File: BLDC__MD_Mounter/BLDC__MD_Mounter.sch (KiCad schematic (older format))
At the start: 0 parts

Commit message: Placed Connectors on schematic
for Motor Driver, BLDC, Control and Power.
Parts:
- added J? (x8): Conn_02x07_Odd_Even, symbol Connector_Generic:Conn_02x07_Odd_Even
- added J? (x4): Conn_01x08_Female, symbol Connector:Conn_01x08_Female
- added J?: Conn_02x10_Odd_Even, symbol Connector_Generic:Conn_02x10_Odd_Even
- added J?: Conn_01x02_Male, symbol Connector:Conn_01x02_Male
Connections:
- new net +3V3: J?.1 (Pin_1), J?.5 (Pin_5), J?.5 (Pin_5), J?.5 (Pin_5), J?.5 (Pin_5)
- new net +5V: J?.10 (Pin_10), J?.10 (Pin_10), J?.10 (Pin_10), J?.10 (Pin_10), J?.3 (Pin_3), J?.6 (Pin_6), J?.6 (Pin_6), J?.6 (Pin_6), J?.6 (Pin_6), J?.9 (Pin_9), J?.9 (Pin_9), J?.9 (Pin_9), J?.9 (Pin_9)
- new net COIL_A_1: J?.5 (Pin_5), J?.6 (Pin_6)
- new net COIL_A_2: J?.5 (Pin_5), J?.6 (Pin_6)
- new net COIL_A_3: J?.5 (Pin_5), J?.6 (Pin_6)
- new net COIL_A_4: J?.5 (Pin_5), J?.6 (Pin_6)
- new net COIL_B_1: J?.10 (Pin_10), J?.9 (Pin_9)
- new net COIL_B_2: J?.10 (Pin_10), J?.9 (Pin_9)
- new net COIL_B_3: J?.10 (Pin_10), J?.9 (Pin_9)
- new net COIL_B_4: J?.10 (Pin_10), J?.9 (Pin_9)
- new net COIL_C_1: J?.7 (Pin_7), J?.8 (Pin_8)
- new net COIL_C_2: J?.7 (Pin_7), J?.8 (Pin_8)
- new net COIL_C_3: J?.7 (Pin_7), J?.8 (Pin_8)
- new net COIL_C_4: J?.7 (Pin_7), J?.8 (Pin_8)
- new net FG_1: J?.1 (Pin_1), J?.11 (Pin_11)
- new net FG_2: J?.1 (Pin_1), J?.19 (Pin_19)
- new net FG_3: J?.1 (Pin_1), J?.14 (Pin_14)
- new net FG_4: J?.1 (Pin_1), J?.6 (Pin_6)
- new net FR_1: J?.2 (Pin_2), J?.9 (Pin_9)
- new net FR_2: J?.17 (Pin_17), J?.2 (Pin_2)
- new net FR_3: J?.16 (Pin_16), J?.2 (Pin_2)
- new net FR_4: J?.2 (Pin_2), J?.8 (Pin_8)
- new net GND: J?.2 (Pin_2), J?.4 (Pin_4), J?.7 (Pin_7), J?.7 (Pin_7), J?.7 (Pin_7), J?.7 (Pin_7), J?.8 (Pin_8), J?.8 (Pin_8), J?.8 (Pin_8), J?.8 (Pin_8), J?.8 (Pin_8), J?.8 (Pin_8), J?.8 (Pin_8), J?.8 (Pin_8)
- new net HALL_A_N_1: J?.3 (Pin_3), J?.4 (Pin_4)
- new net HALL_A_N_2: J?.3 (Pin_3), J?.4 (Pin_4)
- new net HALL_A_N_3: J?.3 (Pin_3), J?.4 (Pin_4)
- new net HALL_A_N_4: J?.3 (Pin_3), J?.4 (Pin_4)
- new net HALL_A_P_1: J?.3 (Pin_3), J?.4 (Pin_4)
- new net HALL_A_P_2: J?.3 (Pin_3), J?.4 (Pin_4)
- new net HALL_A_P_3: J?.3 (Pin_3), J?.4 (Pin_4)
- new net HALL_A_P_4: J?.3 (Pin_3), J?.4 (Pin_4)
- new net HALL_B_N_1: J?.5 (Pin_5), J?.6 (Pin_6)
- new net HALL_B_N_2: J?.5 (Pin_5), J?.6 (Pin_6)
- new net HALL_B_N_3: J?.5 (Pin_5), J?.6 (Pin_6)
- new net HALL_B_N_4: J?.5 (Pin_5), J?.6 (Pin_6)
- new net HALL_B_P_1: J?.11 (Pin_11), J?.12 (Pin_12)
- new net HALL_B_P_2: J?.11 (Pin_11), J?.12 (Pin_12)
- new net HALL_B_P_3: J?.11 (Pin_11), J?.12 (Pin_12)
- new net HALL_B_P_4: J?.11 (Pin_11), J?.12 (Pin_12)
- new net HALL_C_N_1: J?.13 (Pin_13), J?.14 (Pin_14)
- new net HALL_C_N_2: J?.13 (Pin_13), J?.14 (Pin_14)
- new net HALL_C_N_3: J?.13 (Pin_13), J?.14 (Pin_14)
- new net HALL_C_N_4: J?.13 (Pin_13), J?.14 (Pin_14)
- new net HALL_C_P_1: J?.13 (Pin_13), J?.14 (Pin_14)
- new net HALL_C_P_2: J?.13 (Pin_13), J?.14 (Pin_14)
- new net HALL_C_P_3: J?.13 (Pin_13), J?.14 (Pin_14)
- new net HALL_C_P_4: J?.13 (Pin_13), J?.14 (Pin_14)
- new net PWM_1: J?.3 (Pin_3), J?.7 (Pin_7)
- new net PWM_2: J?.15 (Pin_15), J?.3 (Pin_3)
- new net PWM_3: J?.18 (Pin_18), J?.3 (Pin_3)
- new net PWM_4: J?.10 (Pin_10), J?.3 (Pin_3)
- new net RD_1: J?.4 (Pin_4), J?.5 (Pin_5)
- new net RD_2: J?.13 (Pin_13), J?.4 (Pin_4)
- new net RD_3: J?.20 (Pin_20), J?.4 (Pin_4)
- new net RD_4: J?.12 (Pin_12), J?.4 (Pin_4)
- new net VCC: J?.1 (Pin_1), J?.7 (Pin_7), J?.7 (Pin_7), J?.7 (Pin_7), J?.7 (Pin_7)
- no-connect marks 0 -> 25
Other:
- note added: "BLDC"
- note added: "BLDC 1"
- note added: "BLDC 2"
- note added: "BLDC 3"
- note added: "BLDC 4"
- note added: "Control Port"
- note added: "MD Unit 1"
- note added: "MD Unit 2"
- note added: "MD Unit 3"
- note added: "MD Unit 4"
- note added: "Motor Drivers"
- note added: "Power"

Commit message: Added PWR_FLAGs in schematic
connected all Power Symbol to the PWR_FLAG.
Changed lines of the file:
@@
 Text Notes 4000 6050 0    50   ~ 0
 Power
+$Comp
+L power:VCC #PWR?
+U 1 1 5F714662
+P 5700 5200
+F 0 "#PWR?" H 5700 5050 50  0001 C CNN
+F 1 "VCC" H 5715 5373 50  0000 C CNN
+F 2 "" H 5700 5200 50  0001 C CNN
+F 3 "" H 5700 5200 50  0001 C CNN
+	1    5700 5200
+	1    0    0    -1
+$EndComp
+$Comp
+L power:+3V3 #PWR?
+U 1 1 5F714D91
+P 6500 5200
+F 0 "#PWR?" H 6500 5050 50  0001 C CNN
+F 1 "+3V3" H 6515 5373 50  0000 C CNN
+F 2 "" H 6500 5200 50  0001 C CNN
+F 3 "" H 6500 5200 50  0001 C CNN
+	1    6500 5200
+	1    0    0    -1
+$EndComp
+$Comp
+L power:+5V #PWR?
+U 1 1 5F715680
+P 6100 5200
+F 0 "#PWR?" H 6100 5050 50  0001 C CNN
+F 1 "+5V" H 6115 5373 50  0000 C CNN
+F 2 "" H 6100 5200 50  0001 C CNN
+F 3 "" H 6100 5200 50  0001 C CNN
+	1    6100 5200
+	1    0    0    -1
+$EndComp
+$Comp
+L power:GND #PWR?
+U 1 1 5F715FC3
+P 6900 5450
+F 0 "#PWR?" H 6900 5200 50  0001 C CNN
+F 1 "GND" H 6905 5277 50  0000 C CNN
+F 2 "" H 6900 5450 50  0001 C CNN
+F 3 "" H 6900 5450 50  0001 C CNN
+	1    6900 5450
+	1    0    0    -1
+$EndComp
+$Comp
+L power:PWR_FLAG #FLG?
+U 1 1 5F716ACC
+P 5700 5450
+F 0 "#FLG?" H 5700 5525 50  0001 C CNN
+F 1 "PWR_FLAG" H 5700 5623 50  0000 C CNN
+F 2 "" H 5700 5450 50  0001 C CNN
+F 3 "~" H 5700 5450 50  0001 C CNN
+	1    5700 5450
+	-1   0    0    1
+$EndComp
+$Comp
+L power:PWR_FLAG #FLG?
+U 1 1 5F7175FE
+P 6100 5450
+F 0 "#FLG?" H 6100 5525 50  0001 C CNN
+F 1 "PWR_FLAG" H 6100 5623 50  0000 C CNN
+F 2 "" H 6100 5450 50  0001 C CNN
+F 3 "~" H 6100 5450 50  0001 C CNN
+	1    6100 5450
+	-1   0    0    1
+$EndComp
+$Comp
+L power:PWR_FLAG #FLG?
+U 1 1 5F7177D3
+P 6500 5450
+F 0 "#FLG?" H 6500 5525 50  0001 C CNN
+F 1 "PWR_FLAG" H 6500 5623 50  0000 C CNN
+F 2 "" H 6500 5450 50  0001 C CNN
+F 3 "~" H 6500 5450 50  0001 C CNN
+	1    6500 5450
+	-1   0    0    1
+$EndComp
+$Comp
+L power:PWR_FLAG #FLG?
+U 1 1 5F717A64
+P 6900 5200
+F 0 "#FLG?" H 6900 5275 50  0001 C CNN
+F 1 "PWR_FLAG" H 6900 5373 50  0000 C CNN
+F 2 "" H 6900 5200 50  0001 C CNN
+F 3 "~" H 6900 5200 50  0001 C CNN
+	1    6900 5200
+	1    0    0    -1
+$EndComp
+Wire Wire Line
+	5700 5200 5700 5450
+Wire Wire Line
+	6100 5200 6100 5450
+Wire Wire Line
+	6500 5200 6500 5450
+Wire Wire Line
+	6900 5200 6900 5450
 $EndSCHEMATC

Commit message: Annotated all parts
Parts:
- gave numbers to parts that had none: 14

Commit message: Related all symbols and footprints
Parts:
- J1, J10, J13, J7: footprint (none) -> Connector_PinSocket_2.54mm:PinSocket_2x07_P2.54mm_Vertical
- J11, J14, J4, J8: footprint (none) -> Connector_PinSocket_2.54mm:PinSocket_1x08_P2.54mm_Vertical
- J12, J2, J6, J9: footprint (none) -> Connector_PinHeader_2.54mm:PinHeader_2x07_P2.54mm_Vertical
- J3: footprint (none) -> Connector_PinHeader_2.54mm:PinHeader_2x10_P2.54mm_Vertical
- J5: footprint (none) -> Connector_JST:JST_VH_B2P-VH_1x02_P3.96mm_Vertical
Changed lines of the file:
@@
 F 0 "J1" H 2050 1817 50  0000 C CNN
 F 1 "Conn_02x07_Odd_Even" H 2050 1726 50  0000 C CNN
-F 2 "" H 2000 1300 50  0001 C CNN
+F 2 "Connector_PinSocket_2.54mm:PinSocket_2x07_P2.54mm_Vertical" H 2000 1300 50  0001 C CNN
 F 3 "~" H 2000 1300 50  0001 C CNN
 	1    2000 1300
@@
 F 0 "J8" H 4392 1925 50  0000 C CNN
 F 1 "Conn_01x08_Female" H 4392 2016 50  0000 C CNN
-F 2 "" H 4500 2550 50  0001 C CNN
+F 2 "Connector_PinSocket_2.54mm:PinSocket_1x08_P2.54mm_Vertical" H 4500 2550 50  0001 C CNN
 F 3 "~" H 4500 2550 50  0001 C CNN
 	1    4500 2550
@@
 F 0 "J7" H 4450 1817 50  0000 C CNN
 F 1 "Conn_02x07_Odd_Even" H 4450 1726 50  0000 C CNN
-F 2 "" H 4400 1300 50  0001 C CNN
+F 2 "Connector_PinSocket_2.54mm:PinSocket_2x07_P2.54mm_Vertical" H 4400 1300 50  0001 C CNN
 F 3 "~" H 4400 1300 50  0001 C CNN
 	1    4400 1300
@@
 F 0 "J11" H 6792 1925 50  0000 C CNN
 F 1 "Conn_01x08_Female" H 6792 2016 50  0000 C CNN
-F 2 "" H 6900 2550 50  0001 C CNN
+F 2 "Connector_PinSocket_2.54mm:PinSocket_1x08_P2.54mm_Vertical" H 6900 2550 50  0001 C CNN
 F 3 "~" H 6900 2550 50  0001 C CNN
 	1    6900 2550
@@
 F 0 "J10" H 6850 1817 50  0000 C CNN
 F 1 "Conn_02x07_Odd_Even" H 6850 1726 50  0000 C CNN
-F 2 "" H 6800 1300 50  0001 C CNN
+F 2 "Connector_PinSocket_2.54mm:PinSocket_2x07_P2.54mm_Vertical" H 6800 1300 50  0001 C CNN
 F 3 "~" H 6800 1300 50  0001 C CNN
 	1    6800 1300
@@
 F 0 "J14" H 9192 1925 50  0000 C CNN
 F 1 "Conn_01x08_Female" H 9192 2016 50  0000 C CNN
-F 2 "" H 9300 2550 50  0001 C CNN
+F 2 "Connector_PinSocket_2.54mm:PinSocket_1x08_P2.54mm_Vertical" H 9300 2550 50  0001 C CNN
 F 3 "~" H 9300 2550 50  0001 C CNN
 	1    9300 2550
@@
 F 0 "J13" H 9250 1817 50  0000 C CNN
 F 1 "Conn_02x07_Odd_Even" H 9250 1726 50  0000 C CNN
-F 2 "" H 9200 1300 50  0001 C CNN
+F 2 "Connector_PinSocket_2.54mm:PinSocket_2x07_P2.54mm_Vertical" H 9200 1300 50  0001 C CNN
 F 3 "~" H 9200 1300 50  0001 C CNN
 	1    9200 1300
@@
 F 0 "J12" H 7750 4467 50  0000 C CNN
 F 1 "Conn_02x07_Odd_Even" H 7750 4376 50  0000 C CNN
-F 2 "" H 7700 3950 50  0001 C CNN
+F 2 "Connector_PinHeader_2.54mm:PinHeader_2x07_P2.54mm_Vertical" H 7700 3950 50  0001 C CNN
 F 3 "~" H 7700 3950 50  0001 C CNN
 	1    7700 3950
@@
 F 0 "J3" H 2050 6217 50  0000 C CNN
 F 1 "Conn_02x10_Odd_Even" H 2050 6126 50  0000 C CNN
-F 2 "" H 2000 5600 50  0001 C CNN
+F 2 "Connector_PinHeader_2.54mm:PinHeader_2x10_P2.54mm_Vertical" H 2000 5600 50  0001 C CNN
 F 3 "~" H 2000 5600 50  0001 C CNN
 	1    2000 5600
@@
 F 0 "J9" H 5850 4467 50  0000 C CNN
 F 1 "Conn_02x07_Odd_Even" H 5850 4376 50  0000 C CNN
-F 2 "" H 5800 3950 50  0001 C CNN
+F 2 "Connector_PinHeader_2.54mm:PinHeader_2x07_P2.54mm_Vertical" H 5800 3950 50  0001 C CNN
 F 3 "~" H 5800 3950 50  0001 C CNN
 	1    5800 3950
@@
 F 0 "J6" H 3950 4467 50  0000 C CNN
 F 1 "Conn_02x07_Odd_Even" H 3950 4376 50  0000 C CNN
-F 2 "" H 3900 3950 50  0001 C CNN
+F 2 "Connector_PinHeader_2.54mm:PinHeader_2x07_P2.54mm_Vertical" H 3900 3950 50  0001 C CNN
 F 3 "~" H 3900 3950 50  0001 C CNN
 	1    3900 3950
@@
 F 0 "J2" H 2050 4467 50  0000 C CNN
 F 1 "Conn_02x07_Odd_Even" H 2050 4376 50  0000 C CNN
-F 2 "" H 2000 3950 50  0001 C CNN
+F 2 "Connector_PinHeader_2.54mm:PinHeader_2x07_P2.54mm_Vertical" H 2000 3950 50  0001 C CNN
 F 3 "~" H 2000 3950 50  0001 C CNN
 	1    2000 3950
@@
 F 0 "J4" H 1992 1925 50  0000 C CNN
 F 1 "Conn_01x08_Female" H 1992 2016 50  0000 C CNN
-F 2 "" H 2100 2550 50  0001 C CNN
+F 2 "Connector_PinSocket_2.54mm:PinSocket_1x08_P2.54mm_Vertical" H 2100 2550 50  0001 C CNN
 F 3 "~" H 2100 2550 50  0001 C CNN
 	1    2100 2550
@@
 F 0 "J5" H 3808 5781 50  0000 C CNN
 F 1 "Conn_01x02_Male" H 3808 5690 50  0000 C CNN
-F 2 "" H 3700 5600 50  0001 C CNN
+F 2 "Connector_JST:JST_VH_B2P-VH_1x02_P3.96mm_Vertical" H 3700 5600 50  0001 C CNN
 F 3 "~" H 3700 5600 50  0001 C CNN
 	1    3700 5600

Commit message: Connected some simple lines
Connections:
- net FG_3: now also J3.6 (Pin_6); no longer J3.14 (Pin_14)
- net FG_4: now also J3.14 (Pin_14); no longer J3.6 (Pin_6)
- net FR_3: now also J3.8 (Pin_8); no longer J3.16 (Pin_16)
- net FR_4: now also J3.16 (Pin_16); no longer J3.8 (Pin_8)
- net PWM_3: now also J3.10 (Pin_10); no longer J3.18 (Pin_18)
- net PWM_4: now also J3.18 (Pin_18); no longer J3.10 (Pin_10)
- net RD_3: now also J3.12 (Pin_12); no longer J3.20 (Pin_20)
- net RD_4: now also J3.20 (Pin_20); no longer J3.12 (Pin_12)
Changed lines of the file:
@@
 	2750 6100 2300 6100
 Text Label 2750 6100 2    50   ~ 0
+RD_4
+Text Label 2750 6000 2    50   ~ 0
+PWM_4
+Text Label 2750 5900 2    50   ~ 0
+FR_4
+Text Label 2750 5800 2    50   ~ 0
+FG_4
+Text Label 2750 5700 2    50   ~ 0
 RD_3
-Text Label 2750 6000 2    50   ~ 0
+Text Label 2750 5600 2    50   ~ 0
 PWM_3
-Text Label 2750 5900 2    50   ~ 0
+Text Label 2750 5500 2    50   ~ 0
 FR_3
-Text Label 2750 5800 2    50   ~ 0
+Text Label 2750 5400 2    50   ~ 0
 FG_3
-Text Label 2750 5700 2    50   ~ 0
-RD_4
-Text Label 2750 5600 2    50   ~ 0
-PWM_4
-Text Label 2750 5500 2    50   ~ 0
-FR_4
-Text Label 2750 5400 2    50   ~ 0
-FG_4
 $Comp
 L power:+5V #PWR0129

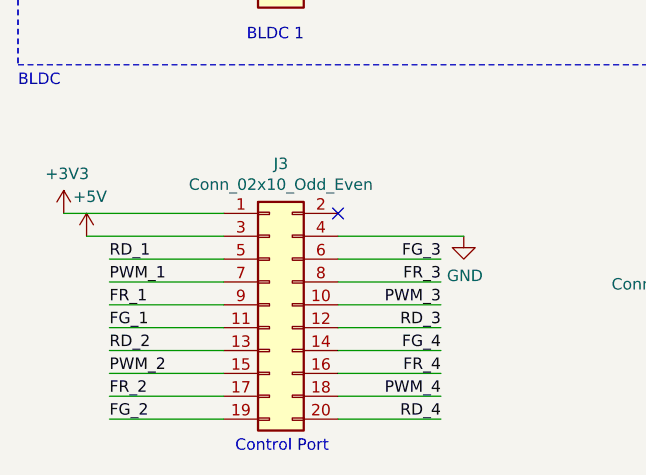
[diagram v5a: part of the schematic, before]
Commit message: #fix reverse pin sockets bottom and sig port pin socket.
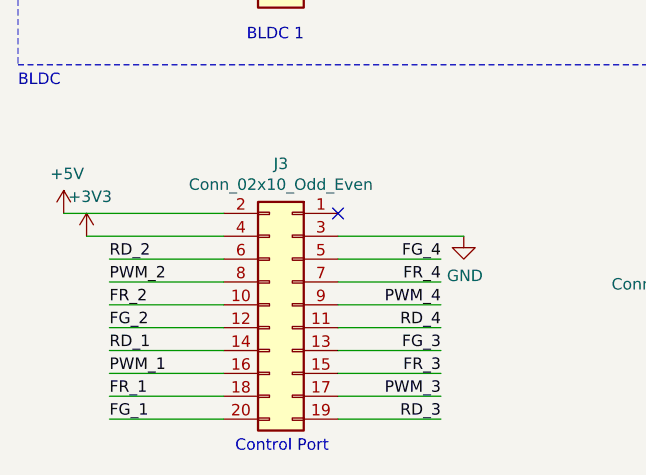
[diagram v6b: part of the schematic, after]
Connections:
- net +3V3: now also J3.4 (Pin_4); no longer J3.1 (Pin_1)
- net +5V: now also J3.2 (Pin_2); no longer J3.3 (Pin_3)
- net FG_1: now also J3.20 (Pin_20); no longer J3.11 (Pin_11)
- net FG_2: now also J3.12 (Pin_12); no longer J3.19 (Pin_19)
- net FG_3: now also J3.13 (Pin_13); no longer J3.6 (Pin_6)
- net FG_4: now also J3.5 (Pin_5); no longer J3.14 (Pin_14)
- net FR_1: now also J3.18 (Pin_18); no longer J3.9 (Pin_9)
- net FR_2: now also J3.10 (Pin_10); no longer J3.17 (Pin_17)
- net FR_3: now also J3.15 (Pin_15); no longer J3.8 (Pin_8)
- net FR_4: now also J3.7 (Pin_7); no longer J3.16 (Pin_16)
- net GND: now also J3.3 (Pin_3); no longer J3.4 (Pin_4)
- net PWM_1: now also J3.16 (Pin_16); no longer J3.7 (Pin_7)
- net PWM_2: now also J3.8 (Pin_8); no longer J3.15 (Pin_15)
- net PWM_3: now also J3.17 (Pin_17); no longer J3.10 (Pin_10)
- net PWM_4: now also J3.9 (Pin_9); no longer J3.18 (Pin_18)
- net RD_1: now also J3.14 (Pin_14); no longer J3.5 (Pin_5)
- net RD_2: now also J3.6 (Pin_6); no longer J3.13 (Pin_13)
- net RD_3: now also J3.19 (Pin_19); no longer J3.12 (Pin_12)
- net RD_4: now also J3.11 (Pin_11); no longer J3.20 (Pin_20)
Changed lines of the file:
@@
 Text Notes 900  3150 0    50   ~ 0
 Motor Drivers
-Text Label 1300 5400 0    50   ~ 0
+Text Label 1300 5800 0    50   ~ 0
 RD_1
-Text Label 1300 5500 0    50   ~ 0
+Text Label 1300 5900 0    50   ~ 0
 PWM_1
-Text Label 1300 5600 0    50   ~ 0
+Text Label 1300 6000 0    50   ~ 0
 FR_1
-Text Label 1300 5700 0    50   ~ 0
-FG_1
-Text Label 1300 5800 0    50   ~ 0
-RD_2
-Text Label 1300 5900 0    50   ~ 0
-PWM_2
-Text Label 1300 6000 0    50   ~ 0
-FR_2
-Text Label 1300 6100 0    50   ~ 0
-FG_2
 Wire Wire Line
 	1300 5600 1800 5600
@@
 L Connector_Generic:Conn_02x10_Odd_Even J3
 U 1 1 5F5B823A
-P 2000 5600
-F 0 "J3" H 2050 6217 50  0000 C CNN
-F 1 "Conn_02x10_Odd_Even" H 2050 6126 50  0000 C CNN
-F 2 "Connector_PinHeader_2.54mm:PinHeader_2x10_P2.54mm_Vertical" H 2000 5600 50  0001 C CNN
-F 3 "~" H 2000 5600 50  0001 C CNN
-	1    2000 5600
-	1    0    0    -1
+P 2100 5600
+F 0 "J3" H 2150 6217 50  0000 C CNN
+F 1 "Conn_02x10_Odd_Even" H 2150 6126 50  0000 C CNN
+F 2 "Connector_PinHeader_2.54mm:PinHeader_2x10_P2.54mm_Vertical" H 2100 5600 50  0001 C CNN
+F 3 "~" H 2100 5600 50  0001 C CNN
+	1    2100 5600
+	-1   0    0    -1
 $EndComp
 Wire Wire Line
@@
 Wire Wire Line
 	2750 6100 2300 6100
-Text Label 2750 6100 2    50   ~ 0
-RD_4
+Text Label 2750 5600 2    50   ~ 0
+PWM_4
+Text Label 2750 5500 2    50   ~ 0
+FR_4
+Text Label 2750 5400 2    50   ~ 0
+FG_4
 Text Label 2750 6000 2    50   ~ 0
-PWM_4
+PWM_3
 Text Label 2750 5900 2    50   ~ 0
-FR_4
+FR_3
 Text Label 2750 5800 2    50   ~ 0
-FG_4
-Text Label 2750 5700 2    50   ~ 0
-RD_3
-Text Label 2750 5600 2    50   ~ 0
-PWM_3
-Text Label 2750 5500 2    50   ~ 0
-FR_3
-Text Label 2750 5400 2    50   ~ 0
 FG_3
 $Comp
 L power:+5V #PWR0129
 U 1 1 5F664472
+P 1100 5200
+F 0 "#PWR0129" H 1100 5050 50  0001 C CNN
+F 1 "+5V" H 1115 5373 50  0000 C CNN
+F 2 "" H 1100 5200 50  0001 C CNN
+F 3 "" H 1100 5200 50  0001 C CNN
+	1    1100 5200
+	1    0    0    -1
+$EndComp
+$Comp
+L power:+3V3 #PWR0130
+U 1 1 5F664AC5
 P 1200 5300
-F 0 "#PWR0129" H 1200 5150 50  0001 C CNN
-F 1 "+5V" H 1215 5473 50  0000 C CNN
+F 0 "#PWR0130" H 1200 5150 50  0001 C CNN
+F 1 "+3V3" H 1215 5473 50  0000 C CNN
 F 2 "" H 1200 5300 50  0001 C CNN
 F 3 "" H 1200 5300 50  0001 C CNN
 	1    1200 5300
-	1    0    0    -1
-$EndComp
-$Comp
-L power:+3V3 #PWR0130
-U 1 1 5F664AC5
-P 1100 5200
-F 0 "#PWR0130" H 1100 5050 50  0001 C CNN
-F 1 "+3V3" H 1115 5373 50  0000 C CNN
-F 2 "" H 1100 5200 50  0001 C CNN
-F 3 "" H 1100 5200 50  0001 C CNN
-	1    1100 5200
 	1    0    0    -1
 $EndComp
@@
 Wire Wire Line
 	6900 5200 6900 5450
+Text Label 1300 5600 0    50   ~ 0
+FR_2
+Text Label 1300 5500 0    50   ~ 0
+PWM_2
+Text Label 1300 5400 0    50   ~ 0
+RD_2
+Text Label 2750 5700 2    50   ~ 0
+RD_4
+Text Label 2750 6100 2    50   ~ 0
+RD_3
+Text Label 1300 6100 0    50   ~ 0
+FG_1
+Text Label 1300 5700 0    50   ~ 0
+FG_2
 $EndSCHEMATC
